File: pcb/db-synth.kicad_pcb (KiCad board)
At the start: 2 copper layers, 47 x 36.6 mm, 30 parts, among them J1 Pin Socket 1x4, J2 JST XH 3P, J3 JST XH 2P, J4 JST XH 2P, J5 JST XH 2P, J6 JST XH 3P, U1 AVR128DB28 or AVR64DB28, U2 6N137

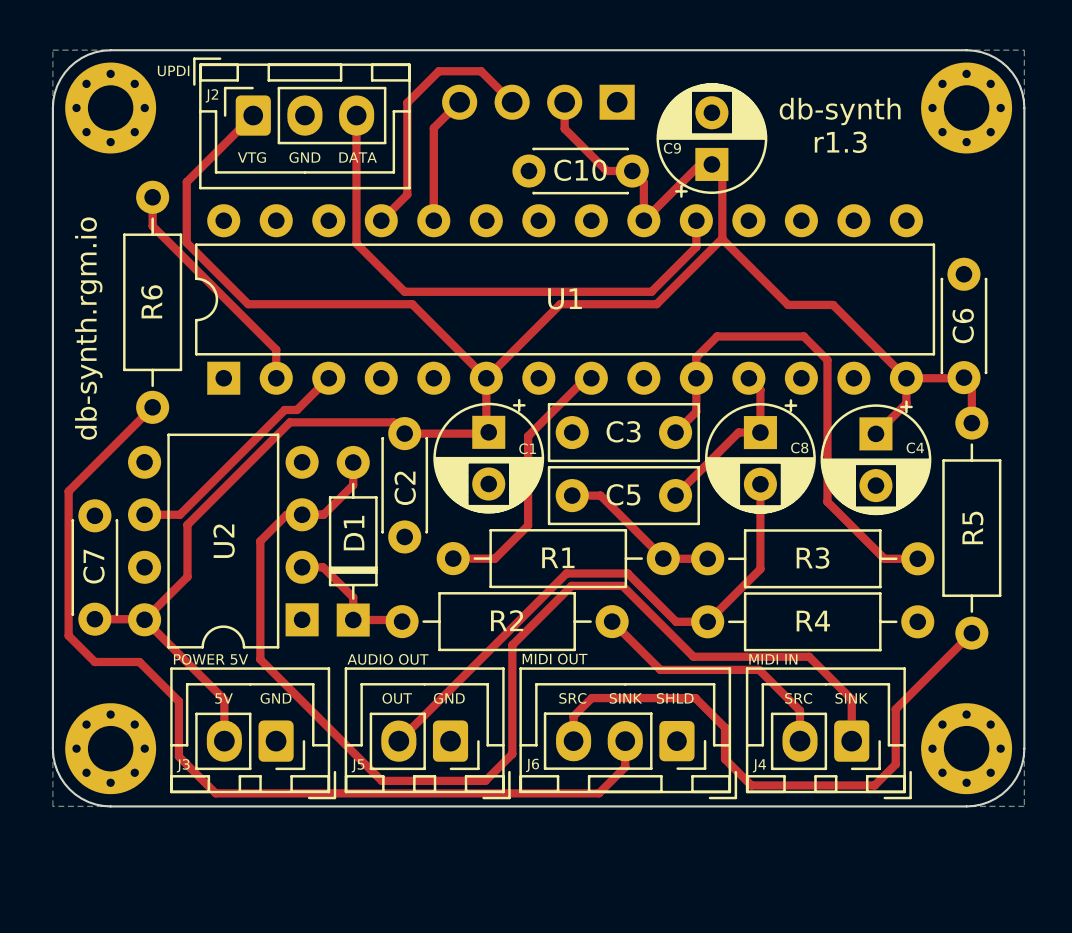
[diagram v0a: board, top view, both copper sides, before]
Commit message: pcb: new revision: 20240111
this revision adds a connector for a reset button, two test points for
development, allows usage of better capacitors, replaces our custom AVR
symbol with a new one from kicad 7 and adds new 3d models.
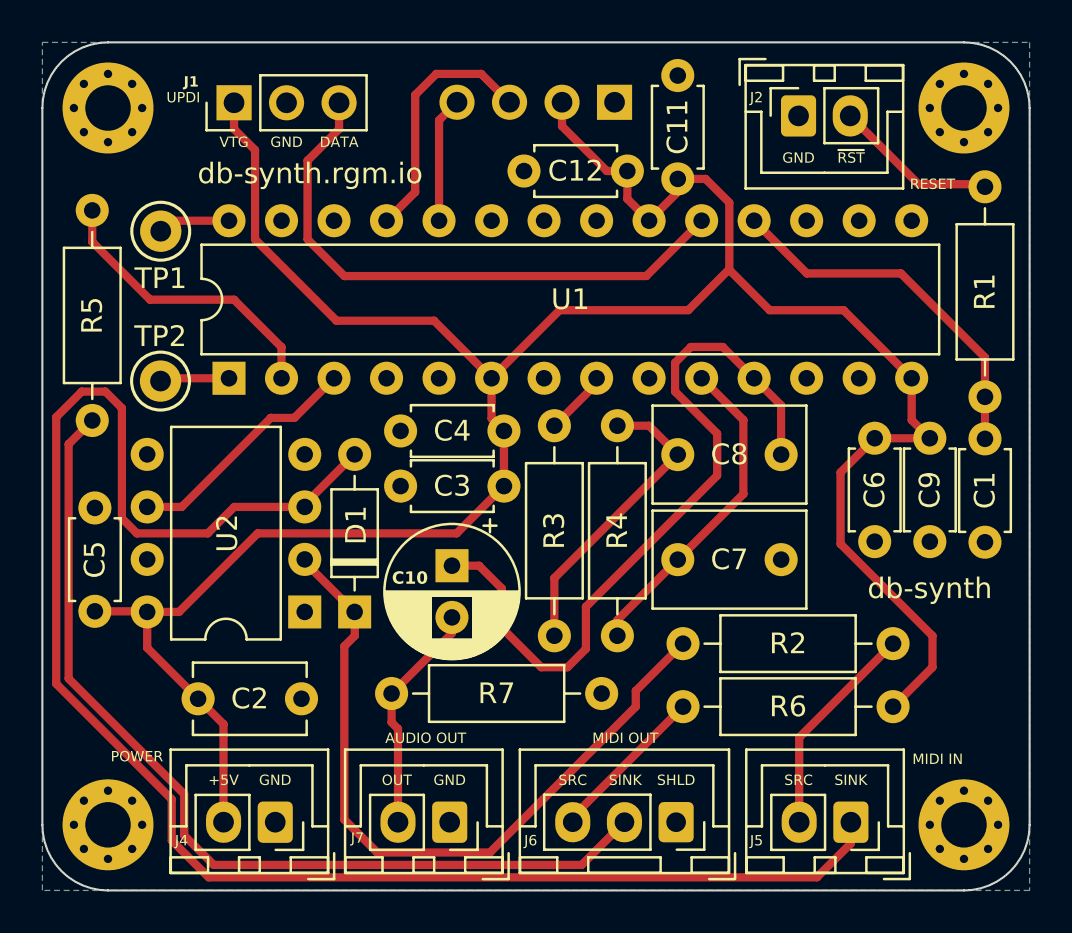
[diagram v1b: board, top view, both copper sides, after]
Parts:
- added C1: 1u, db-synth:C_TDK_FA28, F.Cu at (175.4, 103.2)
- added C2: 10u, db-synth:C_TDK_FA26, F.Cu at (142.3, 110.7)
- added J2: JST XH 2P, db-synth:JST_XH_B2B-XH-A_PinSocket_1x02_P2.50mm_Vertical, F.Cu at (166.4, 82.5)
- added R1: 330R, db-synth:R_YAGEO_MFR-25FTE52_Horizontal, F.Cu at (175.4, 96.1)
- added TP1: PA6, db-synth:TestPoint_Keystone_5001_Miniature, F.Cu at (135.5, 88.1)
- added TP2: PA7, db-synth:TestPoint_Keystone_5001_Miniature, F.Cu at (135.5, 95.4)
- C10: renamed from C8; footprint Capacitor_THT:CP_Radial_D5.0mm_P2.50mm -> Capacitor_THT:CP_Radial_D6.3mm_P2.50mm
- C11: renamed from C9; value 10u -> 1u; footprint Capacitor_THT:CP_Radial_D5.0mm_P2.50mm -> db-synth:C_TDK_FA28
- C12: renamed from C10; footprint Capacitor_THT:C_Disc_D4.3mm_W1.9mm_P5.00mm -> db-synth:C_TDK_FA28
- C3: renamed from C1; value 10u -> 1u; footprint Capacitor_THT:CP_Radial_D5.0mm_P2.50mm -> db-synth:C_TDK_FA28
- C4: renamed from C2; footprint Capacitor_THT:C_Disc_D4.3mm_W1.9mm_P5.00mm -> db-synth:C_TDK_FA28
- C5: renamed from C7; footprint Capacitor_THT:C_Disc_D4.3mm_W1.9mm_P5.00mm -> db-synth:C_TDK_FA28
- C6: renamed from C4; value 10u -> 1u; footprint Capacitor_THT:CP_Radial_D5.0mm_P2.50mm -> db-synth:C_TDK_FA28
- C7: renamed from C3; footprint Capacitor_THT:C_Rect_L7.0mm_W2.5mm_P5.00mm -> Capacitor_THT:C_Rect_L7.2mm_W4.5mm_P5.00mm_FKS2_FKP2_MKS2_MKP2
- C8: renamed from C5; footprint Capacitor_THT:C_Rect_L7.0mm_W2.5mm_P5.00mm -> Capacitor_THT:C_Rect_L7.2mm_W4.5mm_P5.00mm_FKS2_FKP2_MKS2_MKP2
- C9: renamed from C6; footprint Capacitor_THT:C_Disc_D4.3mm_W1.9mm_P5.00mm -> db-synth:C_TDK_FA28
- J1: renamed from J2; value JST XH 3P -> Pin Header 1x3; footprint Connector_JST_with_PinSocket:JST_XH_B3B-XH-A_PinSocket_1x03_P2.50mm_Vertical -> Connector_PinHeader_2.54mm:PinHeader_1x03_P2.54mm_Vertical
- J4: renamed from J3; footprint Connector_JST_with_PinSocket:JST_XH_B2B-XH-A_PinSocket_1x02_P2.50mm_Vertical -> db-synth:JST_XH_B2B-XH-A_PinSocket_1x02_P2.50mm_Vertical
- J5: renamed from J4; footprint Connector_JST_with_PinSocket:JST_XH_B2B-XH-A_PinSocket_1x02_P2.50mm_Vertical -> db-synth:JST_XH_B2B-XH-A_PinSocket_1x02_P2.50mm_Vertical
- J6: footprint Connector_JST_with_PinSocket:JST_XH_B3B-XH-A_PinSocket_1x03_P2.50mm_Vertical -> db-synth:JST_XH_B3B-XH-A_PinSocket_1x03_P2.50mm_Vertical
- J7: renamed from J5; footprint Connector_JST_with_PinSocket:JST_XH_B2B-XH-A_PinSocket_1x02_P2.50mm_Vertical -> db-synth:JST_XH_B2B-XH-A_PinSocket_1x02_P2.50mm_Vertical
- R2: footprint Resistor_THT:R_Axial_DIN0207_L6.3mm_D2.5mm_P10.16mm_Horizontal -> db-synth:R_YAGEO_MFR-25FTE52_Horizontal
- R3: renamed from R1; footprint Resistor_THT:R_Axial_DIN0207_L6.3mm_D2.5mm_P10.16mm_Horizontal -> db-synth:R_YAGEO_MFR-25FTE52_Horizontal
- R4: renamed from R3; footprint Resistor_THT:R_Axial_DIN0207_L6.3mm_D2.5mm_P10.16mm_Horizontal -> db-synth:R_YAGEO_MFR-25FTE52_Horizontal
- R5: renamed from R6; footprint Resistor_THT:R_Axial_DIN0207_L6.3mm_D2.5mm_P10.16mm_Horizontal -> db-synth:R_YAGEO_MFR-25FTE52_Horizontal
- R6: renamed from R5; footprint Resistor_THT:R_Axial_DIN0207_L6.3mm_D2.5mm_P10.16mm_Horizontal -> db-synth:R_YAGEO_MFR-25FTE52_Horizontal
- R7: renamed from R4; footprint Resistor_THT:R_Axial_DIN0207_L6.3mm_D2.5mm_P10.16mm_Horizontal -> db-synth:R_YAGEO_MFR-25FTE52_Horizontal
- U1: value AVR128DB28 or AVR64DB28 -> AVR64DB28x-xSP
- moved C10 16.3 mm to (149.6, 104.3)
- moved R7 15.7 mm to (156.8, 110.5)
- moved R6 14.4 mm to (160.8, 111.1), turned to 0 degrees
- moved R2 13.6 mm to (160.8, 108.1)
- moved R3 8.08 mm to (154.6, 97.5), turned to -90 degrees
- moved R4 7.78 mm to (157.6, 97.5), turned to -90 degrees
- moved C7 6.15 mm to (160.5, 104.0), turned to 0 degrees
- moved C8 5.48 mm to (160.5, 98.9)
- moved C4 4.80 mm to (152.1, 97.8), turned to 180 degrees
- moved REF** 4.38 mm to (165.9, 109.6)
- moved J4 3.92 mm to (141.1, 116.7)
- moved J5 3.92 mm to (168.9, 116.7)
- moved J6 3.92 mm to (160.4, 116.7)
- moved J7 3.92 mm to (149.5, 116.7)
- moved H3 3.69 mm to (133.0, 116.8)
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- renumbered J1 to J3
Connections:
- net Net-(J2-Pin_3) renamed UPDI
- U1 pad 1: unconnected-(U1-PA7-Pad1) -> TP2
- U1 pad 18: unconnected-(U1-PF6/~{RESET}-Pad18) -> RESET
- U1 pad 28: unconnected-(U1-PA6-Pad28) -> TP1
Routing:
- net Net-(D1-K): track 6.56 -> 35.5 mm
- net OPAMP_OUT: track 8.22 -> 36.3 mm
- net Net-(D1-A): track 55.8 -> 80.7 mm
- net Net-(J6-Pin_3): track 28.1 -> 7.96 mm
- net RESET: track 0.00 -> 17.7 mm
- net Net-(J7-Pin_2): track 27.0 -> 11.2 mm
- net VCC: track 110.2 -> 124.5 mm
- net DAC_OUT: track 12.8 -> 3.14 mm
- net Net-(J2-Pin_2): track 0.00 -> 7.88 mm
- net OPAMP_INP: track 23.7 -> 15.8 mm
- net Net-(C8-Pad1): track 7.83 -> 14.7 mm
- net TP1: track 0.00 -> 3.51 mm
- net TP2: track 0.00 -> 3.37 mm
- net MIDI_TX: track 11.2 -> 14.3 mm
- net UPDI: track 25.8 -> 28.1 mm
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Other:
- board size 47 x 36.6 mm -> 47.8 x 41 mm
- board text added: "${COMMENT4}"
- board text added: "Rev.: ${REVISION}"
- board text added: "db-synth"
- board text removed: "db-synth r1.3"

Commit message: pcb: upgrade to kicad 8
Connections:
- U2 pad 4: (no net) -> unconnected-(U2-NC-Pad4)
